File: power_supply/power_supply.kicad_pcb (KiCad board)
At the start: 2 copper layers, 43 parts, among them J1 Conn_01x04_Male, J2 Conn_01x03_Male, J3 Conn_01x03_Male, J4 Conn_01x03_Male, U1 LM7815_TO220, U2 LM7915_TO220, U3 LM7805_TO220

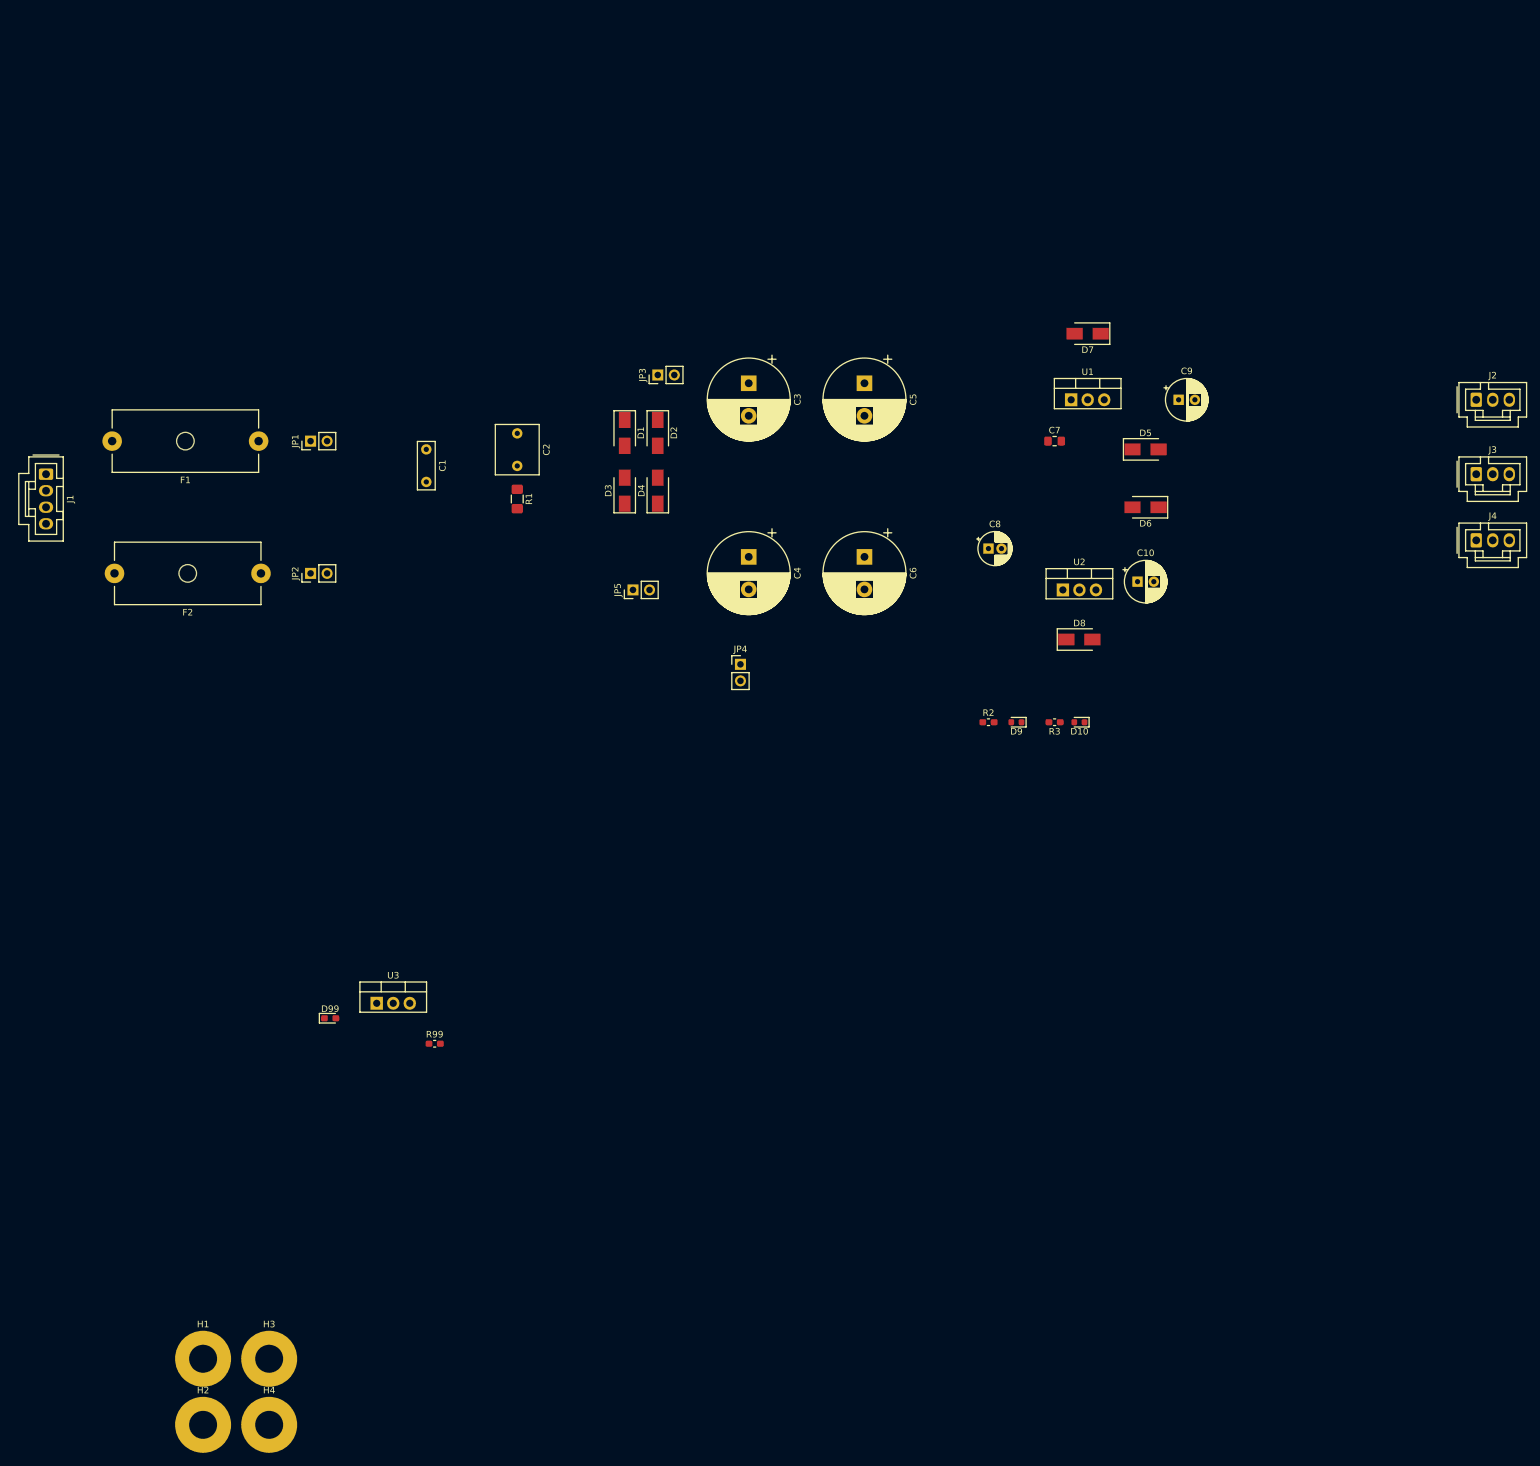
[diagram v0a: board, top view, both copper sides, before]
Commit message: add aux (relay/front panel power supply) to schematics/pcb. Also cleanup DRC violations in schematic
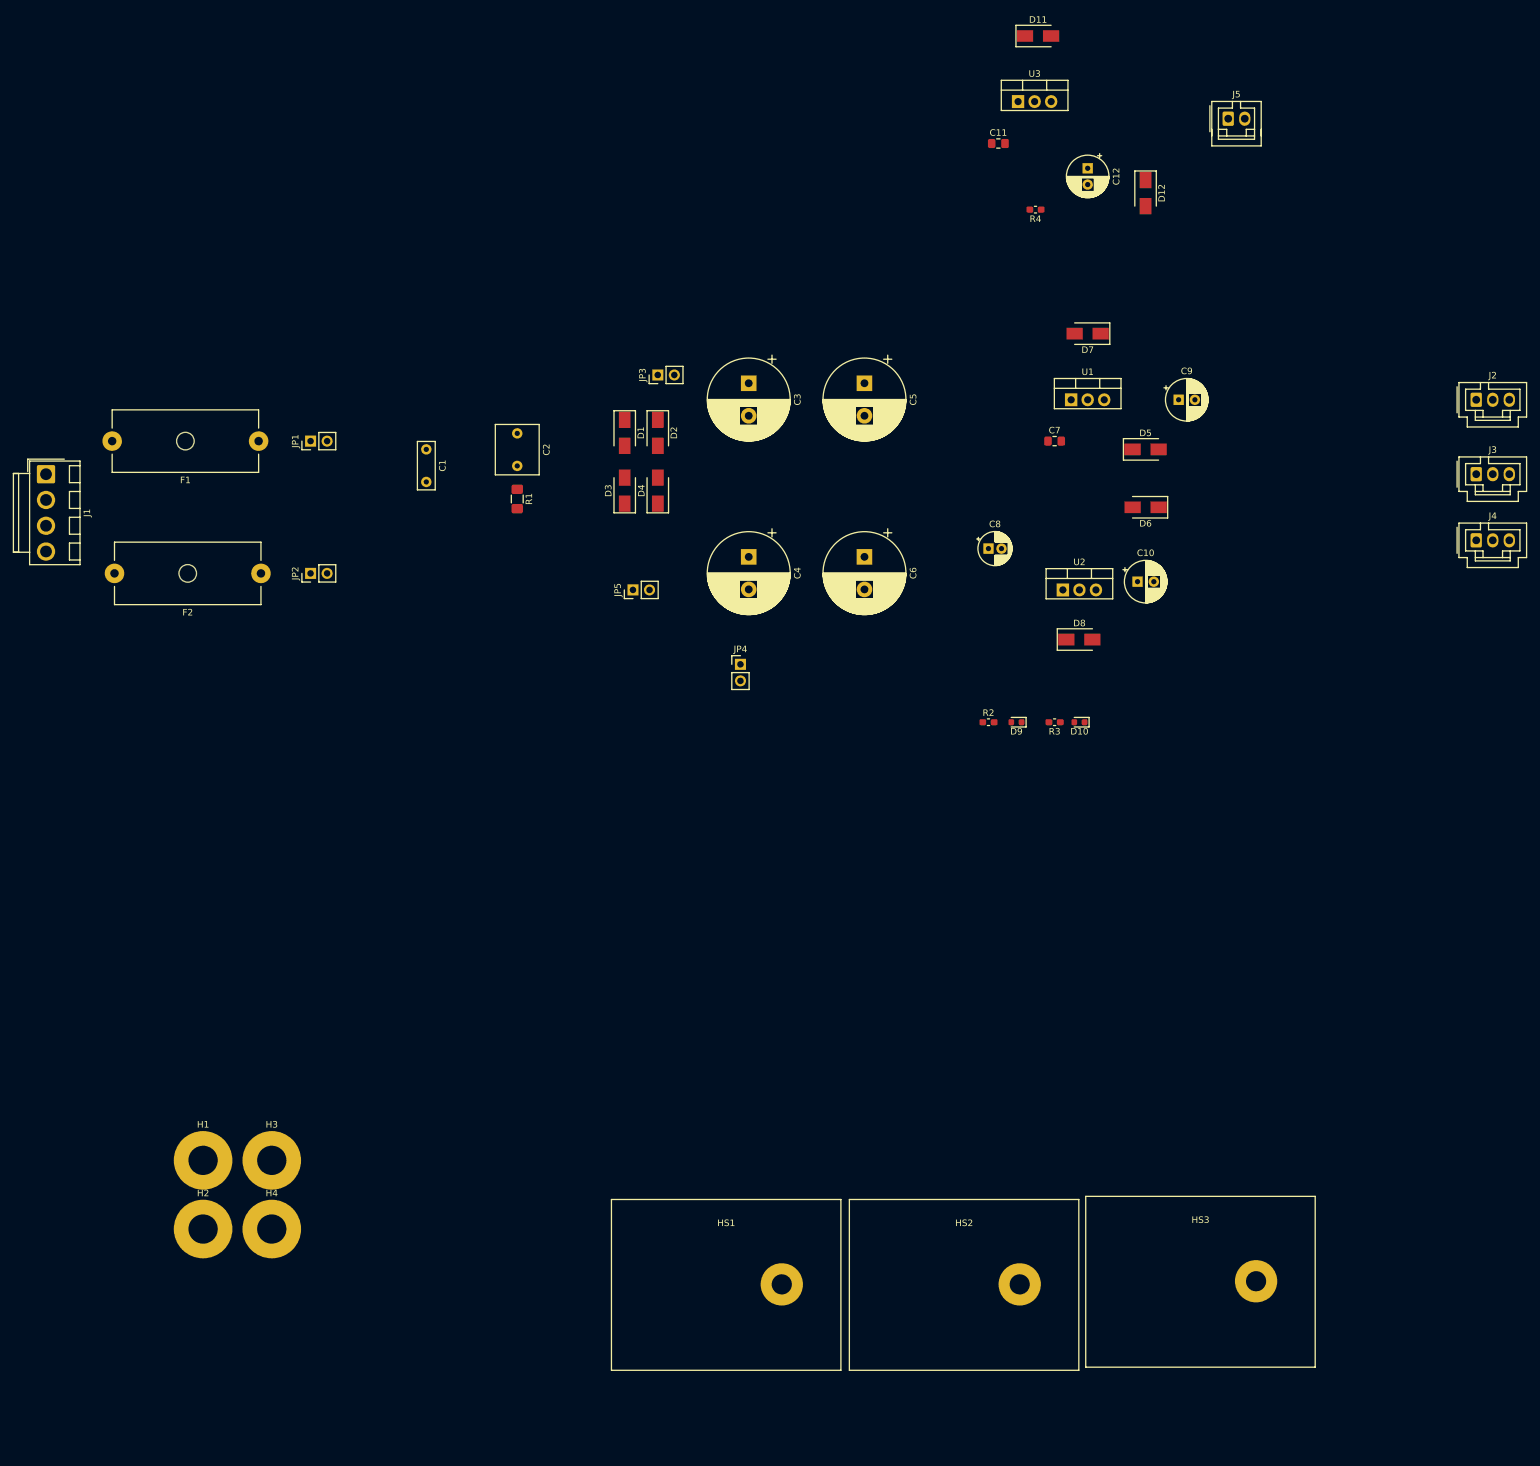
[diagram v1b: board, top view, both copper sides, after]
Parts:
- removed D99: LED_ALT, LED_SMD:LED_0603_1608Metric_Pad1.05x0.95mm_HandSolder
- removed R99: R, Resistor_SMD:R_0603_1608Metric_Pad1.05x0.95mm_HandSolder
- added C11: 330n, Capacitor_SMD:C_0805_2012Metric_Pad1.15x1.40mm_HandSolder, F.Cu at (167.9, -7.62)
- added C12: 100u, Capacitor_THT:CP_Radial_D6.3mm_P2.50mm, F.Cu at (181.6, -3.81)
- added D11: MRA4004T3G, Diode_SMD:D_SMA, F.Cu at (174.0, -24.1)
- added D12: MRA4004T3G, Diode_SMD:D_SMA, F.Cu at (190.5, 0.00)
- added HS1: Heatsink_Pad, Heatsink:Heatsink_35x26mm_1xFixation3mm_Fischer-SK486-35, F.Cu at (134.6, 167.6)
- added HS2: Heatsink_Pad, Heatsink:Heatsink_35x26mm_1xFixation3mm_Fischer-SK486-35, F.Cu at (171.2, 167.6)
- added HS3: Heatsink_Pad, Heatsink:Heatsink_35x26mm_1xFixation3mm_Fischer-SK486-35, F.Cu at (207.5, 167.2)
- added J5: Conn_01x02_Male, Connector_Molex_SL:Molex_SL_A-70543-0001_1x02_P2.54mm_Vertical, F.Cu at (203.2, -11.4)
- added R4: 1k, Resistor_SMD:R_0603_1608Metric_Pad1.05x0.95mm_HandSolder, F.Cu at (173.6, 2.54)
- H1, H2, H3, H4: footprint MountingHole:MountingHole_4.3mm_M4_Pad -> MountingHole:MountingHole_4.5mm_Pad
- J1: footprint Connector_Molex_SL:Molex_SL_A-70543-0003_1x04_P2.54mm_Vertical -> Connector_Molex_KK-396:Molex_KK-396_A-41791-0004_1x04_P3.96mm_Vertical
- U3: value LM7805_TO220 -> LM7815_TO220
- moved U3 170.0 mm to (170.9, -14.1)
- moved H3 30.5 mm to (56.3, 148.6)
- moved H1 30.5 mm to (45.7, 148.6)
- moved H4 30.1 mm to (56.3, 159.1)
- moved H2 30.1 mm to (45.7, 159.1)
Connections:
- C10 pad 1: GNDPWR -> GNDA
- C3 pad 1: Net-(C3-Pad1) -> /+15_unreg
- C3 pad 2: GNDPWR -> GNDA
- C4 pad 1: GNDPWR -> GNDA
- C4 pad 2: Net-(C4-Pad2) -> /-15_unreg
- C5 pad 1: Net-(C3-Pad1) -> /+15_unreg
- C5 pad 2: GNDPWR -> GNDA
- C6 pad 1: GNDPWR -> GNDA
- C6 pad 2: Net-(C4-Pad2) -> /-15_unreg
- C7 pad 1: Net-(C3-Pad1) -> /+15_unreg
- C7 pad 2: GNDPWR -> GNDA
- C8 pad 1: GNDPWR -> GNDA
- C8 pad 2: Net-(C4-Pad2) -> /-15_unreg
- C9 pad 2: GNDPWR -> GNDA
- D10 pad 1: VEE -> /-15_unreg
- D5 pad 1: Net-(C3-Pad1) -> /+15_unreg
- D6 pad 2: Net-(C4-Pad2) -> /-15_unreg
- D7 pad 2: GNDPWR -> GNDA
- D8 pad 1: GNDPWR -> GNDA
- D9 pad 1: GNDPWR -> GNDA
- H1 pad 1: Net-(H1-Pad1) -> GNDA
- H2 pad 1: Net-(H2-Pad1) -> GNDA
- H3 pad 1: Net-(H3-Pad1) -> GNDA
- H4 pad 1: Net-(H4-Pad1) -> GNDA
- J2 pad 2: GNDPWR -> GNDA
- J3 pad 2: GNDPWR -> GNDA
- J4 pad 2: GNDPWR -> GNDA
- JP3 pad 2: Net-(C3-Pad1) -> /+15_unreg
- JP4 pad 2: GNDPWR -> GNDA
- JP5 pad 2: Net-(C4-Pad2) -> /-15_unreg
- R2 pad 1: VCC -> /+15_unreg
- R3 pad 1: Net-(D10-Pad2) -> GNDA
- R3 pad 2: GNDPWR -> Net-(D10-Pad2)
- U1 pad 1: Net-(C3-Pad1) -> /+15_unreg
- U1 pad 2: GNDPWR -> GNDA
- U2 pad 1: GNDPWR -> GNDA
- U2 pad 2: Net-(C4-Pad2) -> /-15_unreg
- U3 pad 1: Net-(U3-Pad1) -> /+15_unreg
- U3 pad 2: Net-(U3-Pad2) -> GNDD
- U3 pad 3: Net-(U3-Pad3) -> +15V

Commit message: continued preliminary placement
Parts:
- HS1, HS2, HS3: footprint Heatsink:Heatsink_35x26mm_1xFixation3mm_Fischer-SK486-35 -> Heatsink_gkeeth:Heatsink_Wakefield-Vette_287-1AB_T0-220_Vertical
- moved HS3 181.0 mm to (160.6, -7.70)
- moved HS1 133.9 mm to (168.7, 38.1)
- moved HS2 100.4 mm to (167.6, 67.3)
- moved D2 35.4 mm to (82.5, 49.5), turned to 0 degrees
- moved D4 34.9 mm to (82.5, 57.1), turned to 180 degrees
- moved JP3 32.9 mm to (94.6, 53.3)
- moved D1 29.3 mm to (82.5, 45.7), turned to 0 degrees
- moved D3 29.0 mm to (82.5, 53.3), turned to 180 degrees
- moved C2 23.9 mm to (71.8, 45.8)
- moved R1 23.9 mm to (71.8, 55.9)
- moved JP5 22.9 mm to (94.6, 45.7)
- moved C1 16.5 mm to (64.8, 45.7)
- moved D5 6.87 mm to (183.9, 37.6)
- moved C9 5.73 mm to (201.2, 30.5)
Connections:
- net +15V renamed Vrelay
- C11 pad 2: GNDD -> GNDRELAY
- C12 pad 2: GNDD -> GNDRELAY
- D12 pad 2: GNDD -> GNDRELAY
- HS1 pad 1: GNDA -> (no net)
- HS2 pad 1: GNDA -> (no net)
- HS3 pad 1: GNDD -> (no net)
- J5 pad 2: GNDD -> GNDRELAY
- R4 pad 1: GNDD -> GNDRELAY
- U3 pad 2: GNDD -> GNDRELAY
